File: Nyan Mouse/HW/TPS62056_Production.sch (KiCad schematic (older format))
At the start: 7 parts, among them U201 TPS6205X

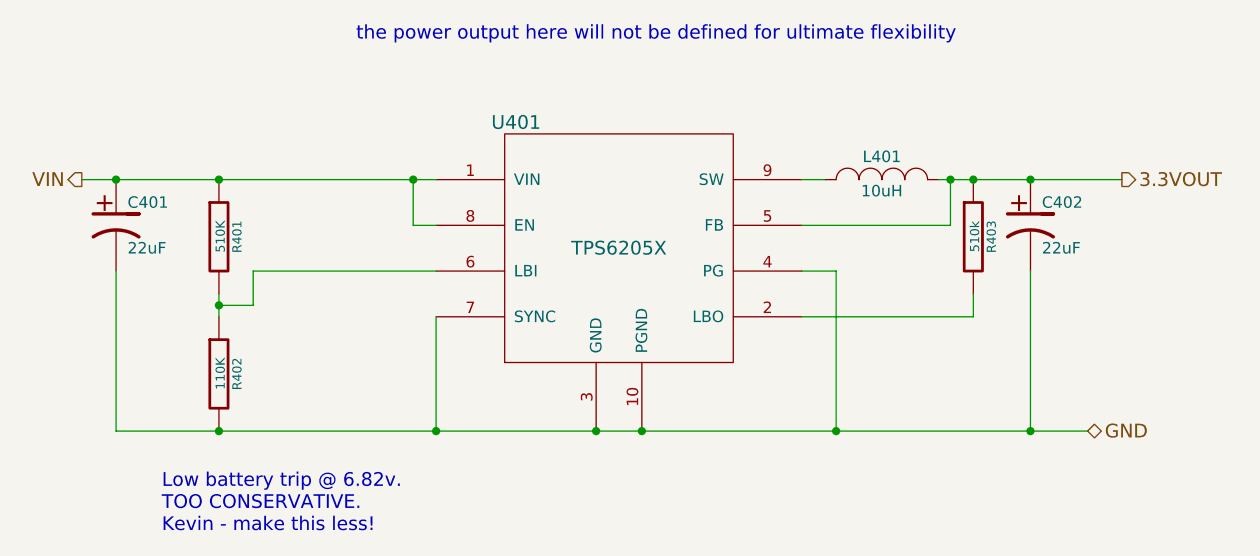
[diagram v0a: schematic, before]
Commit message: Added ESD prevention documentation.
Added ByteBlaster documentation.

Modified FPGA banks.
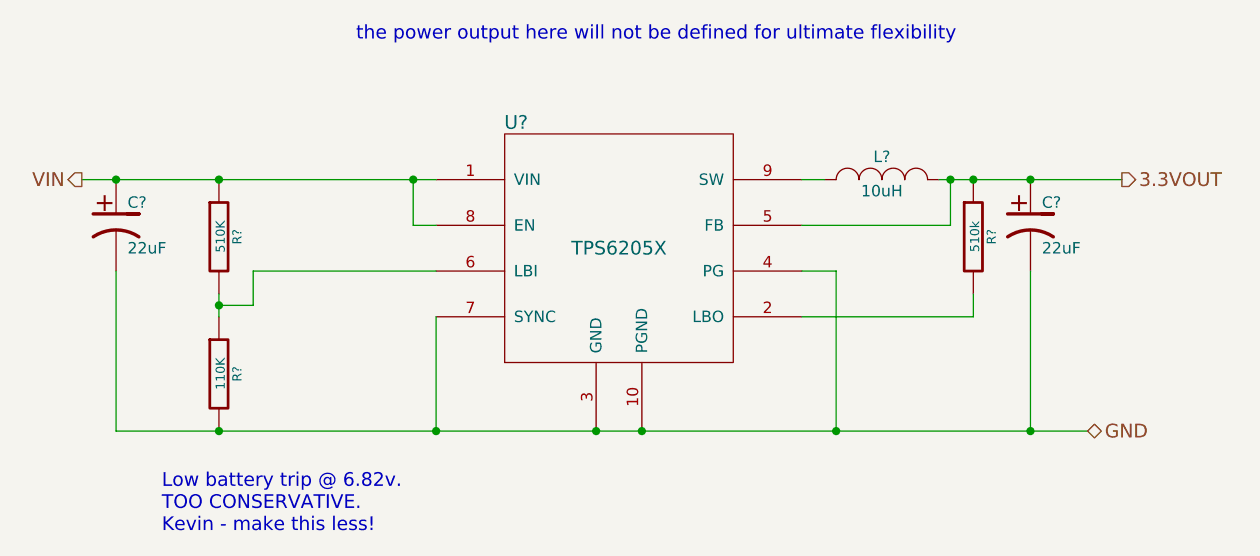
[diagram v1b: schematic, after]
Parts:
- removed C201, C202: 22uF, symbol CP1
- removed L201: 10uH, symbol INDUCTOR_SMALL
- removed R201: 510K, symbol R
- removed R202: 110K, symbol R
- removed R203: 510k, symbol R
- removed U201: TPS6205X, symbol TPS6205X
- added C? (x2): 22uF, symbol CP1
- added L?: 10uH, symbol INDUCTOR_SMALL
- added R?: 510K, symbol R
- added R?: 110K, symbol R
- added R?: 510k, symbol R
- added U?: TPS6205X, symbol TPS6205X
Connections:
- net 3.3VOUT: now also C?.1, L?.2, R?.1, U?.5 (FB)
- net GND: now also C?.2, C?.2, R?.2, U?.10 (PGND), U?.3 (GND), U?.4 (PG), U?.7 (SYNC)
- net VIN: now also C?.1, R?.1, U?.1 (VIN), U?.8 (EN)
- new net: R?.2, U?.2 (LBO)
- new net: R?.1, R?.2, U?.6 (LBI)
- new net: L?.1, U?.9 (SW)
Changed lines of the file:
@@
 LIBS:contrib
 LIBS:valves
+LIBS:tps6205x
+LIBS:stm32f103rx
+LIBS:SparkFun
+LIBS:JST-XH-BattBalance
+LIBS:drv8837
 LIBS:3v3custom
-LIBS:adc128s052
 LIBS:altera_ep4ce15e22c
-LIBS:drv8837
-LIBS:JST-XH-BattBalance
+LIBS:mic94345-4ycs
 LIBS:lp3987
-LIBS:mic94345-4ycs
 LIBS:s25fl064p
-LIBS:SparkFun
-LIBS:stm32f103rx
-LIBS:tps6205x
 LIBS:Nyan Mouse-cache
 EELAYER 24 0
@@
 $Descr USLetter 11000 8500
 encoding utf-8
-Sheet 4 5
+Sheet 3 4
 Title "Nyan Mouse"
-Date "24 apr 2014"
+Date "22 Apr 2014"
 Rev "Alpha"
 Comp "IEEE UCR"
@@
 $EndDescr
 $Comp
-L TPS6205X U201
-U 1 1 535727C9
+L TPS6205X U?
+U 1 1 535478BD
 P 3300 2500
-AR Path="/535488D9/535727C9" Ref="U201"  Part="1"
-AR Path="/53573052/535727C9" Ref="U401"  Part="1"
-F 0 "U401" H 2850 2750 60  0000 C CNN
+AR Path="/53547798/535478BD" Ref="U?"  Part="1"
+AR Path="/535488D9/535478BD" Ref="U?"  Part="1"
+F 0 "U?" H 2850 2750 60  0000 C CNN
 F 1 "TPS6205X" H 3300 2200 60  0000 C CNN
 F 2 "" H 2500 2650 60  0000 C CNN
@@
 $EndComp
 $Comp
-L CP1 C201
-U 1 1 535727CA
+L CP1 C?
+U 1 1 5354790A
 P 1100 2700
-AR Path="/535488D9/535727CA" Ref="C201"  Part="1"
-AR Path="/53573052/535727CA" Ref="C401"  Part="1"
-F 0 "C401" H 1150 2800 50  0000 L CNN
+AR Path="/53547798/5354790A" Ref="C?"  Part="1"
+AR Path="/535488D9/5354790A" Ref="C?"  Part="1"
+F 0 "C?" H 1150 2800 50  0000 L CNN
 F 1 "22uF" H 1150 2600 50  0000 L CNN
 F 2 "" H 1100 2700 60  0000 C CNN
@@
 $EndComp
 $Comp
-L R R201
-U 1 1 535727CB
+L R R?
+U 1 1 5354793A
 P 1550 2750
-AR Path="/535488D9/535727CB" Ref="R201"  Part="1"
-AR Path="/53573052/535727CB" Ref="R401"  Part="1"
-F 0 "R401" V 1630 2750 40  0000 C CNN
+AR Path="/53547798/5354793A" Ref="R?"  Part="1"
+AR Path="/535488D9/5354793A" Ref="R?"  Part="1"
+F 0 "R?" V 1630 2750 40  0000 C CNN
 F 1 "510K" V 1557 2751 40  0000 C CNN
 F 2 "" V 1480 2750 30  0000 C CNN
@@
 $EndComp
 $Comp
-L R R202
-U 1 1 535727CC
+L R R?
+U 1 1 5354794E
 P 1550 3350
-AR Path="/535488D9/535727CC" Ref="R202"  Part="1"
-AR Path="/53573052/535727CC" Ref="R402"  Part="1"
-F 0 "R402" V 1630 3350 40  0000 C CNN
+AR Path="/53547798/5354794E" Ref="R?"  Part="1"
+AR Path="/535488D9/5354794E" Ref="R?"  Part="1"
+F 0 "R?" V 1630 3350 40  0000 C CNN
 F 1 "110K" V 1557 3351 40  0000 C CNN
 F 2 "" V 1480 3350 30  0000 C CNN
@@
 Connection ~ 3400 3600
 $Comp
-L R R203
-U 1 1 535727CD
+L R R?
+U 1 1 535479CB
 P 4850 2750
-AR Path="/535488D9/535727CD" Ref="R203"  Part="1"
-AR Path="/53573052/535727CD" Ref="R403"  Part="1"
-F 0 "R403" V 4930 2750 40  0000 C CNN
+AR Path="/53547798/535479CB" Ref="R?"  Part="1"
+AR Path="/535488D9/535479CB" Ref="R?"  Part="1"
+F 0 "R?" V 4930 2750 40  0000 C CNN
 F 1 "510k" V 4857 2751 40  0000 C CNN
 F 2 "" V 4780 2750 30  0000 C CNN
@@
 	1100 3600 1100 2900
 $Comp
-L INDUCTOR_SMALL L201
-U 1 1 535727CE
+L INDUCTOR_SMALL L?
+U 1 1 53547A93
 P 4450 2500
-AR Path="/535488D9/535727CE" Ref="L201"  Part="1"
-AR Path="/53573052/535727CE" Ref="L401"  Part="1"
-F 0 "L401" H 4450 2600 50  0000 C CNN
+AR Path="/53547798/53547A93" Ref="L?"  Part="1"
+AR Path="/535488D9/53547A93" Ref="L?"  Part="1"
+F 0 "L?" H 4450 2600 50  0000 C CNN
 F 1 "10uH" H 4450 2450 50  0000 C CNN
 F 2 "" H 4450 2500 60  0000 C CNN
@@
 	5100 2900 5100 3600
 $Comp
-L CP1 C202
-U 1 1 535727CF
+L CP1 C?
+U 1 1 53547BCD
 P 5100 2700
-AR Path="/535488D9/535727CF" Ref="C202"  Part="1"
-AR Path="/53573052/535727CF" Ref="C402"  Part="1"
-F 0 "C402" H 5150 2800 50  0000 L CNN
+AR Path="/53547798/53547BCD" Ref="C?"  Part="1"
+AR Path="/535488D9/53547BCD" Ref="C?"  Part="1"
+F 0 "C?" H 5150 2800 50  0000 L CNN
 F 1 "22uF" H 5150 2600 50  0000 L CNN
 F 2 "" H 5100 2700 60  0000 C CNN
